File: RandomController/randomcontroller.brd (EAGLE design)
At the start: 103 parts, among them IC1 TPS2054B, IC2 TPS2054B, IC3 TPS2054B, IC4 TPS2054B, IC6 PIC16F1939PT, Q1 NX-3215, U1 MCP1700_SOT23

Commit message: random controller first version
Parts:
- removed R10, R11, R12, R13, R14, R15, R16, R17, R18, R19, R20, R21, R22, R8, R9: 10k, WaterDrop:R0805(2012)
- added C15: 0.1uF, WaterDrop:C0805(2012)
- added C16: (no value), yBrainDigital:C1206(3216)-A
- added H1, H2, H3, H4: MOUNT-PAD-ROUND3.2, holes:3,2-PAD
- added LED17: (no value), adafruit:CHIPLED_0805
- added U$1: LOGO, WaterDrop:SSCONTROL
- R7: value 10k -> 2.2k
- moved C9 68.3 mm to (20.0, 73.7), flipped to the bottom, turned to 180 degrees
- moved R1 54.3 mm to (-26.0, 81.9)
- moved C10 51.8 mm to (9.84, 73.7), flipped to the bottom, turned to 180 degrees
- moved C4 50.4 mm to (-27.9, 81.9), turned to 270 degrees
- moved C13 41.9 mm to (9.21, 34.6), turned to 90 degrees
- moved JP3 41.0 mm to (-25.4, 44.5)
- moved D1 39.2 mm to (-20.3, 43.2)
- moved U1 38.4 mm to (-15.9, 39.1), turned to 0 degrees
- moved C1 36.8 mm to (-18.1, 43.2)
- moved C11 35.3 mm to (-0.32, 73.7), flipped to the bottom, turned to 180 degrees
- moved C2 34.3 mm to (-16.5, 35.6), turned to 180 degrees
- moved R43 28.8 mm to (-19.7, 3.81)
- moved R38 27.3 mm to (23.5, 20.3), turned to 90 degrees
- moved JP8 25.4 mm to (-16.5, 3.81)
- moved S1 22.9 mm to (0.00, 6.99)
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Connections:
- removed net N$33: IC1.13, R8.1
- removed net N$34: IC1.12, R9.1
- removed net N$35: IC1.9, R10.1
- removed net N$36: IC2.16, R11.1
- removed net N$37: IC2.13, R12.1
- removed net N$38: IC2.12, R13.1
- removed net N$39: IC2.9, R14.1
- removed net N$40: IC3.16, R15.1
- removed net N$41: IC3.13, R16.1
- removed net N$42: IC3.12, R17.1
- removed net N$43: IC3.9, R18.1
- removed net N$44: IC4.16, R19.1
- removed net N$45: IC4.13, R20.1
- removed net N$46: IC4.12, R21.1
- removed net N$47: IC4.9, R22.1
- net +3.3V: no longer R10.2, R11.2, R12.2, R13.2, R14.2, R15.2, R16.2, R17.2, R18.2, R19.2, R20.2, R21.2, R22.2, R7.2, R8.2, R9.2
- net +5V: now also C15.1, C16.1
- net CLKOUT: now also R7.2
- net GND: now also C15.2, C16.2, LED17.C
- net N$3: no longer D2.1
- net N$32: now also LED17.A; no longer IC1.16
- net N$4: now also D2.1
- net STRUT_GND: now also H1.B3,2, H2.B3,2
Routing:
- net +5V: track 0.00 -> 160.3 mm, vias 0 -> 5
- net +3.3V: track 0.00 -> 121.0 mm, vias 0 -> 3
- net GND: track 0.00 -> 80.0 mm, vias 0 -> 41
- net OUT1: track 0.00 -> 36.3 mm
- net OUT2: track 0.00 -> 33.8 mm
- net OUT3: track 0.00 -> 33.7 mm
- net MODE2_SEL: track 0.00 -> 29.9 mm
- net OUT4: track 0.00 -> 29.9 mm
- net OUT5: track 0.00 -> 29.5 mm
- net OUT16: track 0.00 -> 29.5 mm
- net OUT7: track 0.00 -> 28.8 mm
- net OUT8: track 0.00 -> 28.6 mm
- net OUT6: track 0.00 -> 27.9 mm
- net OUT15: track 0.00 -> 27.7 mm
- net PGC: track 0.00 -> 27.6 mm, vias 0 -> 2
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- added copper zone on layer 1, net GND
- added copper zone on layer 16, net GND
- added copper zone on layer 1, net STRUT_GND
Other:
- board outline added: 60 x 90 mm
- board text added: "1"
- board text added: "10"
- board text added: "11"
- board text added: "12"
- board text added: "13"
- board text added: "14"
- board text added: "15"
- board text added: "16"
- board text added: "2"
- board text added: "3"
- board text added: "4"
- board text added: "5"
- board text added: "5V"
- board text added: "6"
- board text added: "7"
- board text added: "8"
- board text added: "9"
- board text added: "DELAY"
- board text added: "GND"
- board text added: "MODE1"
- board text added: "MODE2"
- board text added: "Master"
- board text added: "ON"
- board text added: "RX"
- board text added: "Slave"
- board text added: "TEST"
- board text added: "TX"

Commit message: waterdrop and random controller gerber
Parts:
- R1: value 1M -> 620k
- R2, R23, R24, R25, R26, R27, R28, R29, R30, R31, R32, R33, R34, R35, R36, R37, R7: value 2.2k -> 1k
- R38: value 10k -> 100k
- R4: value (none) -> 1k
- RN1, RN2: value (none) -> 4.7k
- moved C7 0.32 mm to (0.32, 21.9)
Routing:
- net GND: track 80.0 -> 82.2 mm

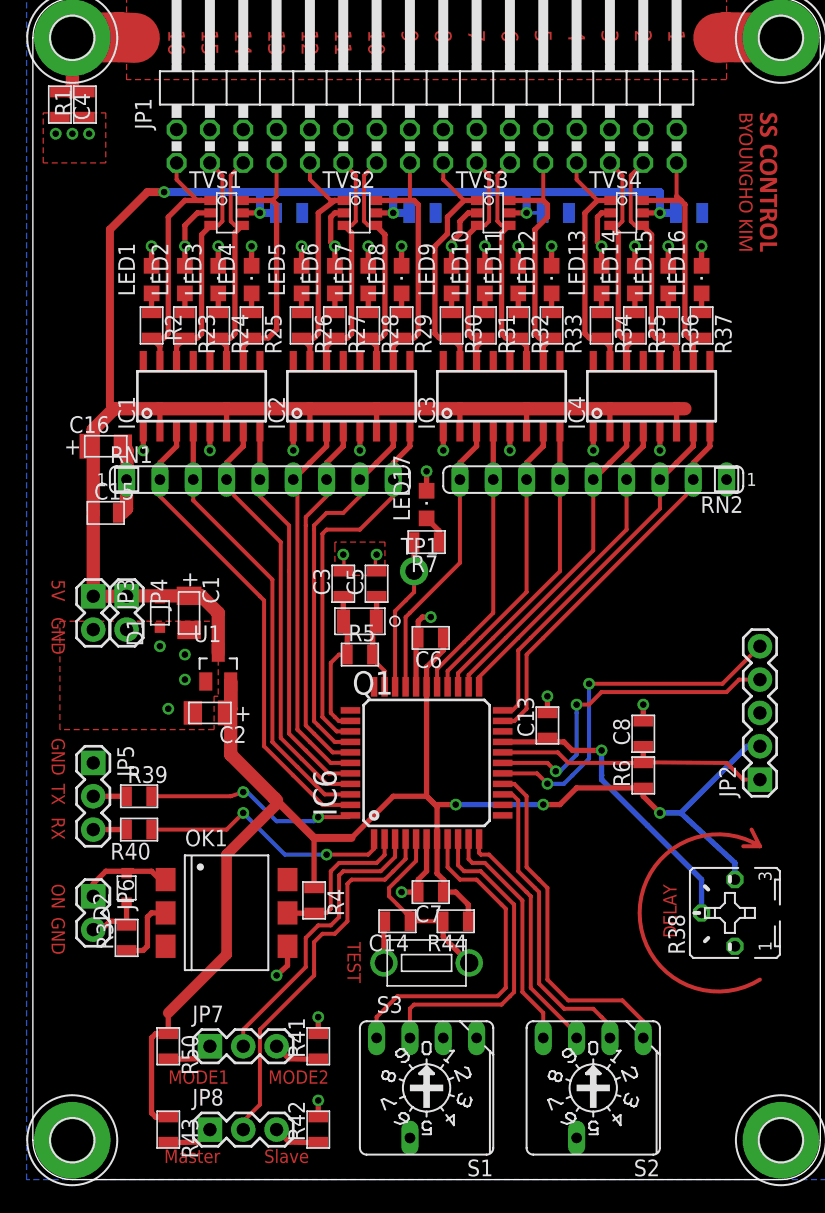
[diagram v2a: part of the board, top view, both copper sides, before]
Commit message: schmatic renumbered final merged gerber for fab
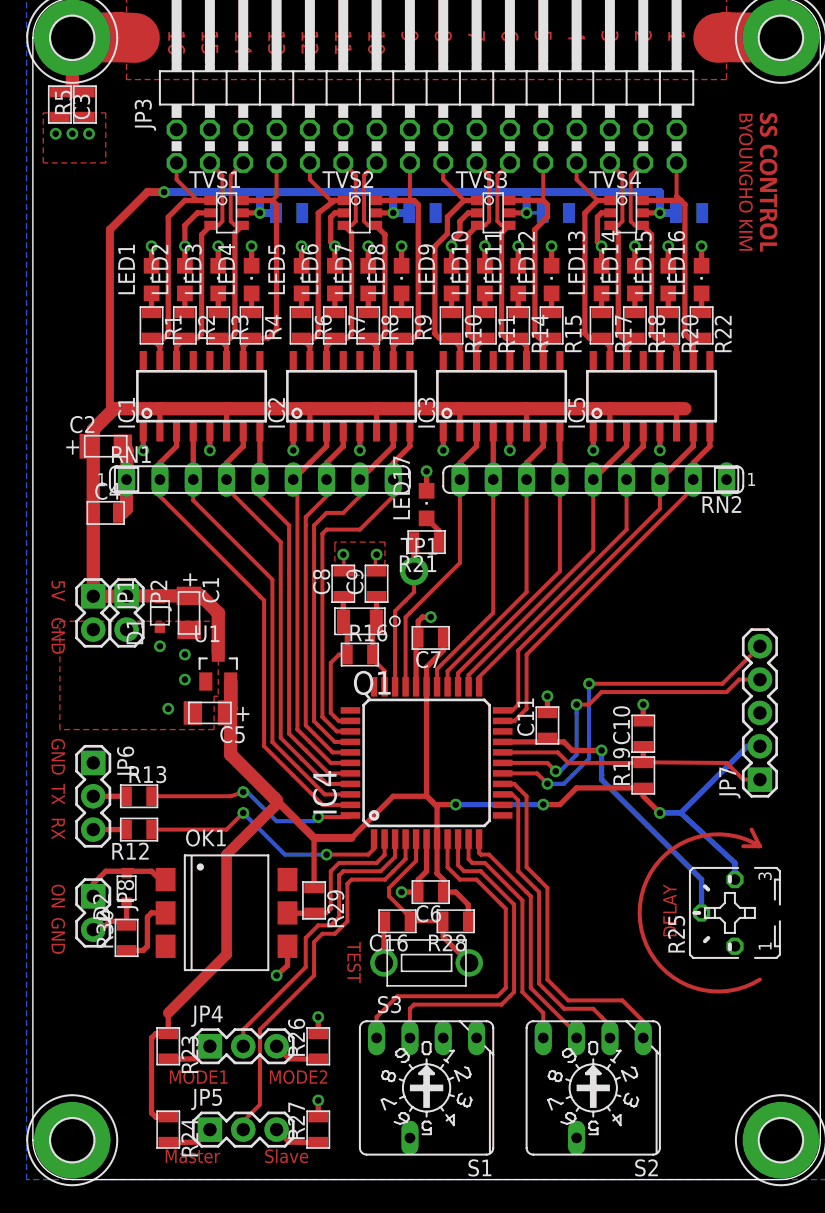
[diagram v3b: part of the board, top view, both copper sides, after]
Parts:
- removed IC6: PIC16F1939PT, microchip:TQFP44
- removed R38: 100k, pot:B25P
- removed R41, R42, R43, R44, R50: 10k, WaterDrop:R0805(2012)
- added IC5: TPS2054B, WaterDrop:R-PDSO-G16
- added R10, R21, R8, R9: 1k, WaterDrop:R0805(2012)
- added R16: DNP, WaterDrop:R0805(2012)
- added R19: 10k, WaterDrop:R0805(2012)
- C16: value (none) -> 0.1uF; device yBrainDigital:C1206(3216)-A -> WaterDrop:C0805(2012)
- C3: value 12.5pF -> 0.1uF
- C5: value 12.5pF -> (none); device WaterDrop:C0805(2012) -> yBrainDigital:C1206(3216)-A
- C8, C9: value 0.1uF -> 12.5pF
- IC4: value TPS2054B -> PIC16F1939PT; device WaterDrop:R-PDSO-G16 -> microchip:TQFP44
- JP1: value (none) -> M02PTH; device pinhead:2X16/90 -> SparkFun-Connectors:1X02
- JP2: value (none) -> M02PTH; device SparkFun-Connectors:1X05 -> SparkFun-Connectors:1X02
- JP3: value M02PTH -> (none); device SparkFun-Connectors:1X02 -> pinhead:2X16/90
- JP4, JP6: value M02PTH -> (none); device SparkFun-Connectors:1X02 -> SparkFun-Connectors:1X03
- JP7: device SparkFun-Connectors:1X03 -> SparkFun-Connectors:1X05
- JP8: value (none) -> M02PTH; device SparkFun-Connectors:1X03 -> SparkFun-Connectors:1X02
- R1: value 620k -> 1k
- R23, R24, R26, R27, R28: value 1k -> 10k
- R25: value 1k -> 100k; device WaterDrop:R0805(2012) -> pot:B25P
- R3: value 220 -> 1k
- R30: value 1k -> 220
- R5: value DNP -> 620k
- R6: value 10k -> 1k
- moved R24 61.4 mm to (-19.7, 3.81)
- moved R27 61.3 mm to (-8.26, 3.81), turned to 90 degrees
- moved R25 58.0 mm to (23.5, 20.3), turned to 90 degrees
- moved C14 55.3 mm to (9.84, 73.7), flipped to the bottom
- moved R23 54.9 mm to (-19.7, 10.2)
- moved R26 54.9 mm to (-8.26, 10.2), turned to 90 degrees
- moved R30 52.8 mm to (-22.9, 18.4), turned to 90 degrees
- moved JP2 50.2 mm to (-22.9, 44.5), turned to 270 degrees
- moved C15 50.0 mm to (20.0, 73.7), flipped to the bottom, turned to 180 degrees
- moved R3 47.2 mm to (-15.9, 65.1), turned to 270 degrees
- moved R5 46.9 mm to (-26.0, 81.9), turned to 90 degrees
- moved JP1 46.9 mm to (-25.4, 44.5), turned to 270 degrees
- moved JP3 46.9 mm to (0.00, 83.8), turned to 0 degrees
- moved JP7 46.6 mm to (25.4, 30.5), turned to 90 degrees
- moved R28 45.9 mm to (2.22, 19.7), turned to 180 degrees
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- renumbered R31 to R11, R32 to R14, R33 to R15, R34 to R17, R35 to R18, R36 to R20, R37 to R22, R39 to R13, R40 to R12
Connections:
- net +3.3V: now also C5.1, IC4.28, IC4.7, JP7.2, R19.1, R23.1, R24.1, R25.E, R28.1, R29.1; no longer C2.1, IC6.28, IC6.7, JP2.2, R38.E, R4.1, R43.1, R44.1, R50.1, R6.1
- net +5V: now also C13.1, C14.1, C2.1, C4.1, IC5.2, IC5.6, JP1.1, JP2.1; no longer C10.1, C11.1, C16.1, C9.1, IC4.2, IC4.6, JP3.1, JP4.1
- net CLKOUT: now also IC4.31, R21.2; no longer IC6.31, R7.2
- net CMD_IN: now also IC4.2, R29.2; no longer IC6.2, R4.2
- net DELAY_ADJ: now also C11.1, IC4.19, R25.S; no longer C13.1, IC6.19, R38.S
- net GND: now also IC4.29, IC4.6, IC5.1, IC5.5, JP2.2, JP3.10, JP3.12, JP3.14, JP3.16, JP3.18, JP3.20, JP3.22, JP3.24, JP3.26, JP3.28, JP3.30, JP3.32, JP3.4, JP3.6, JP3.8, JP6.1, JP7.3, R25.A, R26.2, R27.2, R5.1; no longer IC4.1, IC4.5, IC6.29, IC6.6, JP1.10, JP1.12, JP1.14, JP1.16, JP1.18, JP1.20, JP1.22, JP1.24, JP1.26, JP1.28, JP1.30, JP1.32, JP1.4, JP1.6, JP1.8, JP2.3, JP4.2, JP5.1, R1.1, R38.A, R41.2, R42.2
- net MODE1_SEL: now also IC4.3, JP4.2; no longer IC6.3, JP7.2
- net MODE2_SEL: now also IC4.4, JP5.2; no longer IC6.4, JP8.2
- net N$1: now also JP8.1; no longer JP6.1
- net N$10: now also R6.1; no longer R26.1
- net N$11: now also R7.1; no longer R27.1
- net N$12: now also JP3.1, R1.2; no longer JP1.1, R2.2
- net N$13: now also JP3.3, R2.2; no longer JP1.3, R23.2
- net N$14: now also JP3.5, R3.2; no longer JP1.5, R24.2
- net N$15: now also JP3.7, R4.2; no longer JP1.7, R25.2
- net N$16: now also JP3.9, R6.2; no longer JP1.9, R26.2
- net N$17: now also JP3.11, R7.2; no longer JP1.11, R27.2
- net N$18: now also JP3.13, R8.2; no longer JP1.13, R28.2
- net N$19: now also JP3.15, R9.2; no longer JP1.15, R29.2
- net N$2: now also R1.1; no longer R2.1
- net N$20: now also JP3.19; no longer JP1.19
- net N$21: now also JP3.21; no longer JP1.21
- net N$22: now also JP3.23; no longer JP1.23
- net N$23: now also JP3.17, R10.2; no longer JP1.17, R30.2
- net N$24: now also IC5.14, JP3.27; no longer IC4.14, JP1.27
- net N$25: now also IC5.15, JP3.25; no longer IC4.15, JP1.25
- net N$26: now also IC5.11, JP3.29; no longer IC4.11, JP1.29
- net N$27: now also IC5.10, JP3.31; no longer IC4.10, JP1.31
- net N$28: now also R10.1; no longer R30.1
- net N$3: now also R30.1; no longer R3.1
- net N$32: now also R21.1; no longer R7.1
- net N$4: now also JP8.2, R30.2; no longer JP6.2, R3.2
- net N$5: now also R2.1; no longer R23.1
- net N$52: now also R8.1; no longer R28.1
- net N$53: now also R9.1; no longer R29.1
- net N$54: now also IC4.1; no longer IC6.1
- net N$55: now also IC4.44; no longer IC6.44
- net N$56: now also JP5.1, R24.2; no longer JP8.1, R43.2
- net N$57: now also JP4.1, R23.2; no longer JP7.1, R50.2
- net N$58: now also JP4.3, R26.1; no longer JP7.3, R41.1
- net N$59: now also JP5.3, R27.1; no longer JP8.3, R42.1
- net N$6: now also C8.1, IC4.35, R16.1; no longer C3.1, IC6.35, R5.1
- net N$7: now also C9.1, IC4.32, R16.2; no longer C5.1, IC6.32, R5.2
- net N$8: now also R3.1; no longer R24.1
- net N$9: now also R4.1; no longer R25.1
- net OUT1: now also IC4.43; no longer IC6.43
- net OUT10: now also IC4.27; no longer IC6.27
- net OUT11: now also IC4.26; no longer IC6.26
- net OUT12: now also IC4.25; no longer IC6.25
- net OUT13: now also IC4.24, IC5.3; no longer IC4.3, IC6.24
- net OUT14: now also IC4.23, IC5.4; no longer IC4.4, IC6.23
- net OUT15: now also IC4.22, IC5.7; no longer IC4.7, IC6.22
- net OUT16: now also IC4.21, IC5.8; no longer IC4.8, IC6.21
- net OUT2: now also IC4.42; no longer IC6.42
- net OUT3: now also IC4.41; no longer IC6.41
- net OUT4: now also IC4.40; no longer IC6.40
- net OUT5: now also IC4.39; no longer IC6.39
- net OUT6: now also IC4.38; no longer IC6.38
- net OUT7: now also IC4.37; no longer IC6.37
- net OUT8: now also IC4.36; no longer IC6.36
- net OUT9: now also IC4.30; no longer IC6.30
- net PGC: now also IC4.16, JP7.5; no longer IC6.16, JP2.5
- net PGD: now also IC4.17, JP7.4; no longer IC6.17, JP2.4
- net RS0: now also IC4.8; no longer IC6.8
- net RS1: now also IC4.9; no longer IC6.9
- net RS2: now also IC4.10; no longer IC6.10
- net RS3: now also IC4.11; no longer IC6.11
- net RS4: now also IC4.14; no longer IC6.14
- net RS5: now also IC4.15; no longer IC6.15
- net RXD: now also JP6.3; no longer JP5.3
- net STRUT_GND: now also C3.1, R5.2; no longer C4.1, R1.2
- net TEST: now also C16.1, IC4.5, R28.2; no longer C14.1, IC6.5, R44.2
- net TXD: now also JP6.2; no longer JP5.2
- net VPP: now also C10.1, IC4.18, JP7.1, R19.2; no longer C8.1, IC6.18, JP2.1, R6.2

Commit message: part list added
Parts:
- C1, C2, C5: value (none) -> 10uF
- LED17: value (none) -> Yellow
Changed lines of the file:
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@@
 <element name="U1" library="OSSI" package="SOT23" value="MCP1700_SOT23" x="-15.875" y="39.0525"/>
 <element name="D1" library="WaterDrop" package="SOD-323" value="SD0" x="-20.32" y="43.18" rot="R90"/>
-<element name="C1" library="yBrainDigital" package="C1206(3216)-A" value="" x="-18.0975" y="43.18" rot="R270"/>
-<element name="C5" library="yBrainDigital" package="C1206(3216)-A" value="" x="-16.51" y="35.56" rot="R180"/>
+<element name="C1" library="yBrainDigital" package="C1206(3216)-A" value="10uF" x="-18.0975" y="43.18" rot="R270"/>
+<element name="C5" library="yBrainDigital" package="C1206(3216)-A" value="10uF" x="-16.51" y="35.56" rot="R180"/>
 <element name="OK1" library="optocoupler" package="DIL6-SMD" value="4N35SM" x="-15.24" y="20.32" rot="R270">
 <attribute name="OC_NEWARK" value="67K2285" x="-15.24" y="20.32" size="1.778" layer="27" rot="R270" display="off"/>
@@
 <element name="H4" library="holes" package="3,2-PAD" value="MOUNT-PAD-ROUND3.2" x="27" y="3"/>
 <element name="C4" library="WaterDrop" package="C0805(2012)" value="0.1uF" x="-24.4475" y="50.8"/>
-<element name="C2" library="yBrainDigital" package="C1206(3216)-A" value="" x="-24.4475" y="55.88"/>
+<element name="C2" library="yBrainDigital" package="C1206(3216)-A" value="10uF" x="-24.4475" y="55.88"/>
 <element name="R21" library="WaterDrop" package="R0805(2012)" value="1k" x="0" y="48.5775" rot="R180"/>
-<element name="LED17" library="adafruit" package="CHIPLED_0805" value="" x="0" y="51.435"/>
+<element name="LED17" library="adafruit" package="CHIPLED_0805" value="Yellow" x="0" y="51.435"/>
 <element name="U$1" library="WaterDrop" package="SSCONTROL" value="LOGO" x="23.8125" y="81.28" rot="R270"/>
 </elements>
